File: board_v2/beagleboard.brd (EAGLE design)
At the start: 69.8 x 54.6 mm, 35 parts, among them U1 DWM1000, X1 5566-2, X2 04-JST-B4B-XH-A

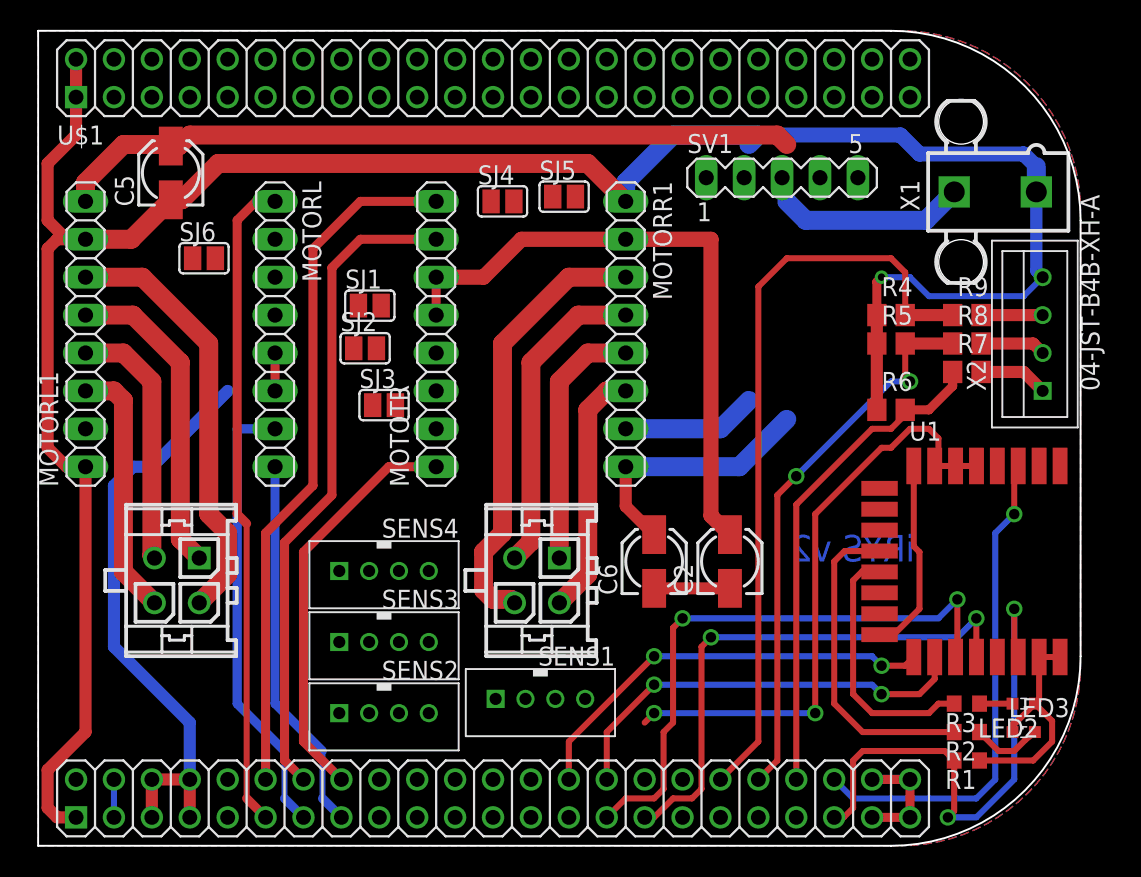
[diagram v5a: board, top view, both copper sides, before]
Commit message: new gpio routed started
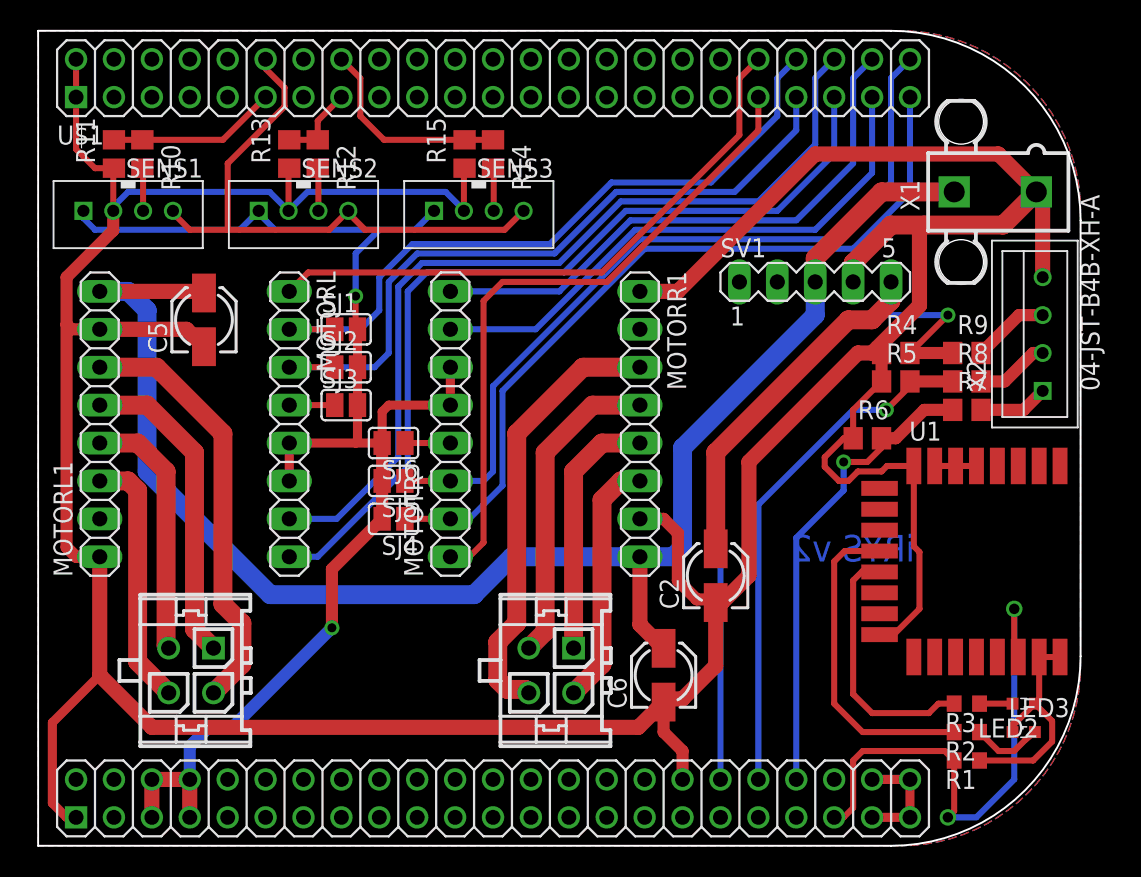
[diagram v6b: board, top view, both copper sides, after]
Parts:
- removed SENS4: 4PIN, libsjst_eph:B4B-PH-K-S
- added R10, R11, R12, R13, R14, R15: (no value), rcl:R0805
- moved SENS1 42.8 mm to (8.57, 43.2)
- moved SENS2 34.1 mm to (20.3, 43.2)
- moved SENS3 29.6 mm to (32.1, 43.2)
- moved SJ4 22.5 mm to (26.4, 22.5), turned to 180 degrees
- moved SJ5 22.2 mm to (26.4, 25.1), turned to 180 degrees
- moved SJ6 17.7 mm to (26.4, 27.6), turned to 180 degrees
- moved C5 10.1 mm to (13.7, 35.9)
- moved C6 7.65 mm to (44.5, 12.1)
- moved SV1 7.33 mm to (54.6, 38.4)
- moved MCONL 6.11 mm to (14.3, 12.4)
- moved MOTORL 6.11 mm to (19.4, 28.9)
- moved MOTORL1 6.11 mm to (6.67, 28.9)
- moved MOTORR1 6.11 mm to (42.9, 28.9)
- moved MOTOTR 6.11 mm to (30.2, 28.9)
- moved MCONR 6.11 mm to (38.4, 12.4)
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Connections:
- net SCL1 renamed N$79
- removed net D1TRIG: SENS1.4, U$1.72
- removed net D2TRIG: SENS2.4, U$1.68
- removed net D3TRIG: SENS3.4
- removed net N$101: U$1.73
- removed net N$24: U$1.12
- removed net N$26: U$1.16
- removed net N$37: U$1.38
- removed net N$38: U$1.40
- removed net N$43: U$1.11
- removed net N$45: U$1.15
- removed net VDD_3V3EXP: U$1.49, U$1.50
- new net LM0: MOTORL.2, SJ1.1, U$1.40
- new net LM1: MOTORL.3, SJ2.1, U$1.39
- new net N$68: U$1.64
- new net N$69: U$1.66
- new net N$70: U$1.78
- new net N$71: U$1.68
- new net N$72: U$1.70
- new net N$73: U$1.72
- new net N$74: U$1.67
- new net N$75: U$1.69
- new net N$76: R10.2, SENS1.3
- new net N$77: U$1.88
- new net N$78: R12.2, SENS2.3
- new net N$80: R14.2, SENS3.3
- new net RM0: MOTOTR.2, SJ4.1, U$1.45
- new net RM1: MOTOTR.3, SJ5.1, U$1.46
- new net TRIG: SENS1.4, SENS2.4, SENS3.4, U$1.12
- net +5V: no longer SENS4.1
- net D1ECHO: now also R10.1, R11.2, U$1.11; no longer SENS1.3, U$1.70
- net D2ECHO: now also R12.1, R13.2, U$1.15; no longer SENS2.3, U$1.67
- net D3ECHO: now also R14.1, R15.2, U$1.16; no longer SENS3.3, U$1.69
- net D4ECHO: no longer SENS4.3
- net D4TRIG: no longer SENS4.4
- net DWMRES: now also U$1.73; no longer U$1.88
- net GND: now also R11.1, R13.1, R15.1; no longer SENS4.2
- net MLDIR: now also U$1.41; no longer U$1.61
- net MLEN: now also U$1.38; no longer U$1.57
- net MLSTEP: now also U$1.42; no longer U$1.59
- net MRDIR: now also U$1.44; no longer U$1.58
- net MREN: now also U$1.37; no longer U$1.62
- net MRSTEP: now also U$1.43; no longer U$1.60
- net N$39: now also U$1.55; no longer U$1.42
- net N$40: now also U$1.49; no longer U$1.44
- net N$41: now also U$1.57; no longer U$1.46
- net N$53: now also U$1.59; no longer MOTORL.3, SJ2.1
- net N$54: now also U$1.61; no longer MOTORL.2, SJ1.1
- net N$55: now also U$1.71; no longer MOTOTR.2, SJ4.1
- net N$60: now also U$1.65; no longer U$1.37
- net N$61: now also U$1.50; no longer U$1.39
- net N$62: now also U$1.56; no longer U$1.41
- net N$63: now also U$1.58; no longer U$1.43
- net N$64: now also U$1.60; no longer U$1.45
- net N$65: now also U$1.62; no longer MOTOTR.3, SJ5.1
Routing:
- net GND: track 219.7 -> 303.8 mm, vias 1 -> 0
- net RM1: track 0.00 -> 53.0 mm
- net RM0: track 0.00 -> 53.0 mm
- net LM1: track 0.00 -> 48.6 mm
- net LM0: track 0.00 -> 47.3 mm
- net MISO: track 39.4 -> 0.00 mm, vias 2 -> 0
- net TRIG: track 0.00 -> 39.3 mm
- net +3V3: track 40.7 -> 2.80 mm, vias 2 -> 0
- net SCK: track 35.9 -> 0.00 mm, vias 2 -> 0
- net +5V: track 84.5 -> 119.3 mm, vias 0 -> 2
- net DWMRES: track 33.5 -> 0.00 mm, vias 1 -> 0
- net MLDIR: track 25.3 -> 58.4 mm
- net MOSI: track 28.6 -> 0.00 mm, vias 2 -> 0
- net CSN: track 28.5 -> 0.00 mm, vias 2 -> 0
- net MLSTEP: track 30.4 -> 58.6 mm
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
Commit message: before logo
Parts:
- moved C6 1.59 mm to (44.5, 13.7)
- moved R3 0.63 mm to (64.8, 9.53)
- moved R2 0.32 mm to (64.8, 7.94)
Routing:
- net +5V: track 119.3 -> 174.5 mm
- net DWMRES: track 0.00 -> 45.0 mm, vias 0 -> 2
- net GND: track 303.8 -> 346.4 mm
- net MISO: track 0.00 -> 29.9 mm, vias 0 -> 2
- net SCK: track 0.00 -> 29.3 mm, vias 0 -> 2
- net CSN: track 0.00 -> 26.7 mm, vias 0 -> 2
- net MOSI: track 0.00 -> 26.4 mm, vias 0 -> 2
- net IRQ: track 36.3 -> 29.6 mm, vias 2 -> 1
- net +12V: track 103.1 -> 101.6 mm
- net N$3: track 21.7 -> 20.4 mm

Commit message: v3gerbers
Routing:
- net N$24: track 0.00 -> 11.9 mm
- net N$94: track 0.00 -> 6.37 mm
- net N$87: track 0.00 -> 6.26 mm
- net N$84: track 0.00 -> 5.10 mm
- net N$86: track 0.00 -> 5.06 mm
- net N$93: track 0.00 -> 4.63 mm
- net N$88: track 0.00 -> 4.44 mm
- net N$82: track 0.00 -> 4.29 mm
- net N$92: track 0.00 -> 4.28 mm
- net N$99: track 0.00 -> 4.10 mm
- net N$97: track 0.00 -> 4.03 mm
- net N$90: track 0.00 -> 4.00 mm
- net N$95: track 0.00 -> 2.83 mm
- net N$91: track 0.00 -> 1.20 mm
- net N$89: track 0.00 -> 1.01 mm
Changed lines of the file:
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@@
 <plain>
 <text x="65.0875" y="19.685" size="1.778" layer="16" rot="MR0">iRYS v2</text>
+<circle x="29.617984375" y="13.93655" radius="0.182878125" width="0.203" layer="1"/>
+<circle x="25.77360625" y="17.704809375" radius="0.18288125" width="0.203" layer="1"/>
+<circle x="23.017965625" y="14.89825" radius="0.18288125" width="0.203" layer="1"/>
 </plain>
 <attributes>
@@
 <contactref element="U1" pad="18"/>
 <contactref element="U$1" pad="76"/>
-<wire x1="40.64" y1="5.08" x2="43.18" y2="7.62" width="0.4064" layer="1"/>
-<wire x1="43.18" y1="7.62" x2="52.705" y2="7.62" width="0.4064" layer="1"/>
+<wire x1="42.545" y1="7.62" x2="52.705" y2="7.62" width="0.4064" layer="1"/>
 <wire x1="52.705" y1="7.62" x2="54.61" y2="9.525" width="0.4064" layer="1"/>
 <via x="54.61" y="9.525" extent="1-16" drill="0.5"/>
@@
 <wire x1="62.5475" y1="11.43" x2="62.5475" y2="13.2175" width="0.4064" layer="1"/>
 <wire x1="62.5475" y1="13.2175" x2="62.615" y2="13.285" width="0.4064" layer="1"/>
+<wire x1="42.545" y1="7.62" x2="40.64" y2="5.715" width="0.4064" layer="1"/>
+<wire x1="40.64" y1="5.715" x2="40.64" y2="5.08" width="0.4064" layer="1"/>
 </signal>
 <signal name="MISO">
@@
 <contactref element="U$1" pad="75"/>
 <wire x1="40.64" y1="2.54" x2="41.91" y2="3.81" width="0.4064" layer="1"/>
-<wire x1="41.91" y1="3.81" x2="41.91" y2="5.3975" width="0.4064" layer="1"/>
-<wire x1="41.91" y1="5.3975" x2="43.4975" y2="6.985" width="0.4064" layer="1"/>
-<wire x1="43.4975" y1="6.985" x2="53.6575" y2="6.985" width="0.4064" layer="1"/>
+<wire x1="41.91" y1="3.81" x2="41.91" y2="5.715" width="0.4064" layer="1"/>
+<wire x1="41.91" y1="5.715" x2="43.18" y2="6.985" width="0.4064" layer="1"/>
+<wire x1="43.18" y1="6.985" x2="53.6575" y2="6.985" width="0.4064" layer="1"/>
 <wire x1="53.6575" y1="6.985" x2="54.61" y2="7.9375" width="0.4064" layer="1"/>
 <via x="54.61" y="7.9375" extent="1-16" drill="0.5"/>
@@
 <contactref element="U$1" pad="63"/>
 </signal>
+<signal name="N$24">
+<wire x1="26.068834375" y1="11.081559375" x2="27.72505625" y2="12.73778125" width="0.203" layer="1"/>
+<wire x1="25.42225625" y1="11.081559375" x2="26.068834375" y2="11.081559375" width="0.203" layer="1" curve="89.999169"/>
+<wire x1="23.80165625" y1="12.702171875" x2="25.42225625" y2="11.081559375" width="0.203" layer="1"/>
+<wire x1="23.80165625" y1="13.34875" x2="23.80165625" y2="12.702171875" width="0.203" layer="1" curve="89.999169"/>
+<wire x1="25.457865625" y1="15.004959375" x2="23.80165625" y2="13.34875" width="0.203" layer="1"/>
+<wire x1="26.104446875" y1="15.004959375" x2="25.457865625" y2="15.004959375" width="0.203" layer="1" curve="90.001108"/>
+<wire x1="27.72505625" y1="13.384359375" x2="26.104446875" y2="15.004959375" width="0.203" layer="1"/>
+<wire x1="27.72505625" y1="12.73778125" x2="27.725059375" y2="13.384359375" width="0.203" layer="1" curve="89.999446"/>
+</signal>
+<signal name="N$82">
+<wire x1="23.772896875" y1="14.57063125" x2="22.56428125" y2="15.584865625" width="0.203" layer="1" curve="146.914761"/>
+<wire x1="22.367325" y1="15.781821875" x2="22.367328125" y2="15.78181875" width="0.203" layer="1"/>
+<wire x1="22.367328125" y1="15.78181875" x2="22.564284375" y2="15.584859375" width="0.203" layer="1"/>
+<wire x1="23.977515625" y1="14.366009375" x2="22.367328125" y2="15.78181875" width="0.203" layer="1" curve="155.383151"/>
+<wire x1="23.772896875" y1="14.57063125" x2="23.977515625" y2="14.366009375" width="0.203" layer="1"/>
+</signal>
+<signal name="N$84">
+<wire x1="29.41035625" y1="13.492109375" x2="29.783984375" y2="11.81728125" width="0.203" layer="1"/>
+<wire x1="29.41035625" y1="13.492109375" x2="29.86963125" y2="13.5136125" width="0.203" layer="1" curve="73.688236"/>
+<wire x1="29.869634375" y1="12.066121875" x2="29.869634375" y2="13.513609375" width="0.203" layer="1"/>
+<wire x1="30.54470625" y1="12.066121875" x2="29.869634375" y2="12.066121875" width="0.203" layer="1"/>
+<wire x1="29.783984375" y1="11.81728125" x2="30.54470625" y2="12.066121875" width="0.203" layer="1"/>
+</signal>
+<signal name="N$86">
+<wire x1="30.018525" y1="13.655221875" x2="31.536884375" y2="13.655221875" width="0.203" layer="1"/>
+<wire x1="30.018525" y1="13.655221875" x2="30.061296875" y2="14.128709375" width="0.203" layer="1" curve="60.848028"/>
+<wire x1="31.702725" y1="13.75865" x2="30.061296875" y2="14.128709375" width="0.203" layer="1"/>
+<wire x1="31.536884375" y1="13.023071875" x2="31.702725" y2="13.75865" width="0.203" layer="1"/>
+<wire x1="31.536884375" y1="13.655221875" x2="31.536884375" y2="13.023071875" width="0.203" layer="1"/>
+</signal>
+<signal name="N$87">
+<wire x1="28.533275" y1="13.546" x2="30.479975" y2="15.4927" width="0.203" layer="1"/>
+<wire x1="28.338275" y1="13.741" x2="28.533275" y2="13.546" width="0.203" layer="1"/>
+<wire x1="30.39595625" y1="15.79868125" x2="28.338275" y2="13.741" width="0.203" layer="1"/>
+<wire x1="30.479975" y1="15.4927" x2="30.39595625" y2="15.79868125" width="0.203" layer="1"/>
+</signal>
+<signal name="N$88">
+<wire x1="27.944196875" y1="14.135090625" x2="29.319896875" y2="15.510790625" width="0.203" layer="1"/>
+<wire x1="27.750215625" y1="14.329059375" x2="27.944196875" y2="14.135090625" width="0.203" layer="1"/>
+<wire x1="29.125925" y1="15.704771875" x2="27.750215625" y2="14.329059375" width="0.203" layer="1"/>
+<wire x1="29.319896875" y1="15.510790625" x2="29.125925" y2="15.704771875" width="0.203" layer="1"/>
+</signal>
+<signal name="N$89">
+<wire x1="28.134865625" y1="16.494690625" x2="27.12655625" y2="16.49469375" width="0.203" layer="1" curve="89.999645"/>
+</signal>
+<signal name="N$90">
+<wire x1="26.34705625" y1="15.732221875" x2="27.12655625" y2="16.494690625" width="0.203" layer="1"/>
+<wire x1="26.153084375" y1="15.926190625" x2="26.34705625" y2="15.732221875" width="0.203" layer="1"/>
+<wire x1="27.57555625" y1="17.348671875" x2="26.153084375" y2="15.926190625" width="0.203" layer="1"/>
+<wire x1="27.772096875" y1="17.157290625" x2="27.57555625" y2="17.348671875" width="0.203" layer="1"/>
+<wire x1="27.526475" y1="16.90505" x2="27.772096875" y2="17.157290625" width="0.203" layer="1"/>
+</signal>
+<signal name="N$91">
+<wire x1="28.53305625" y1="16.248859375" x2="27.526475" y2="16.905046875" width="0.203" layer="1" curve="90.000662"/>
+</signal>
+<signal name="N$92">
+<wire x1="28.37200625" y1="15.66043125" x2="28.533053125" y2="16.248859375" width="0.203" layer="1" curve="55.807989"/>
+<wire x1="27.395425" y1="14.68385" x2="28.37200625" y2="15.66043125" width="0.203" layer="1"/>
+<wire x1="27.193134375" y1="14.886140625" x2="27.395425" y2="14.68385" width="0.203" layer="1"/>
+<wire x1="28.134865625" y1="15.82788125" x2="27.193134375" y2="14.886140625" width="0.203" layer="1"/>
+<wire x1="28.134865625" y1="15.82788125" x2="28.13486875" y2="16.494690625" width="0.203" layer="1" curve="89.999463"/>
+</signal>
+<signal name="N$93">
+<wire x1="25.18710625" y1="15.704071875" x2="23.764634375" y2="17.12655" width="0.203" layer="1"/>
+<wire x1="24.972234375" y1="15.4892" x2="25.18710625" y2="15.704071875" width="0.203" layer="1"/>
+<wire x1="23.549765625" y1="16.911671875" x2="24.972234375" y2="15.4892" width="0.203" layer="1"/>
+<wire x1="23.764634375" y1="17.12655" x2="23.549765625" y2="16.911671875" width="0.203" layer="1"/>
+</signal>
+<signal name="N$94">
+<wire x1="21.926025" y1="15.00635" x2="20.773415625" y2="16.15895" width="0.203" layer="1"/>
+<wire x1="23.126065625" y1="13.8063" x2="23.8133" y2="14.1422875" width="0.203" layer="1" curve="40.800305"/>
+<wire x1="23.20770625" y1="13.724671875" x2="23.126065625" y2="13.8063" width="0.203" layer="1"/>
+<wire x1="22.993425" y1="13.510390625" x2="23.20770625" y2="13.724671875" width="0.203" layer="1"/>
+<wire x1="20.80965625" y1="15.694171875" x2="22.993425" y2="13.510390625" width="0.203" layer="1"/>
+<wire x1="20.773415625" y1="16.15895" x2="20.80965625" y2="15.694171875" width="0.203" layer="1"/>
+</signal>
+<signal name="N$95">
+<wire x1="22.168446875" y1="15.592759375" x2="21.926021875" y2="15.00635" width="0.203" layer="1" curve="33.613513"/>
+<wire x1="22.363725" y1="15.39748125" x2="22.168446875" y2="15.592759375" width="0.203" layer="1"/>
+<wire x1="22.363725" y1="15.39748125" x2="23.619234375" y2="14.336340625" width="0.203" layer="1" curve="174.284233"/>
+<wire x1="23.813296875" y1="14.142290625" x2="23.619234375" y2="14.336340625" width="0.203" layer="1"/>
+</signal>
+<signal name="N$97">
+<wire x1="26.644325" y1="17.037071875" x2="25.204696875" y2="18.6430875" width="0.203" layer="1" curve="158.713286"/>
+<wire x1="26.451915625" y1="17.238809375" x2="26.644325" y2="17.037071875" width="0.203" layer="1"/>
+<wire x1="26.451915625" y1="17.238809375" x2="25.400159375" y2="18.43815625" width="0.203" layer="1" curve="151.475997"/>
+</signal>
+<signal name="N$98">
+<wire x1="25.204696875" y1="18.643090625" x2="25.40015625" y2="18.438159375" width="0.203" layer="1"/>
+</signal>
+<signal name="N$99">
+<wire x1="24.988946875" y1="18.471840625" x2="26.45139375" y2="16.84189375" width="0.203" layer="1" curve="172.497187"/>
+<wire x1="25.178434375" y1="18.273171875" x2="24.988946875" y2="18.471840625" width="0.203" layer="1"/>
+<wire x1="25.178434375" y1="18.273171875" x2="26.260890625" y2="17.04163125" width="0.203" layer="1" curve="169.987487"/>
+</signal>
+<signal name="N$100">
+<wire x1="26.451396875" y1="16.841890625" x2="26.260896875" y2="17.041621875" width="0.203" layer="1"/>
+</signal>
 </signals>
